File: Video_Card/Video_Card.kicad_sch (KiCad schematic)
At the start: 0 parts

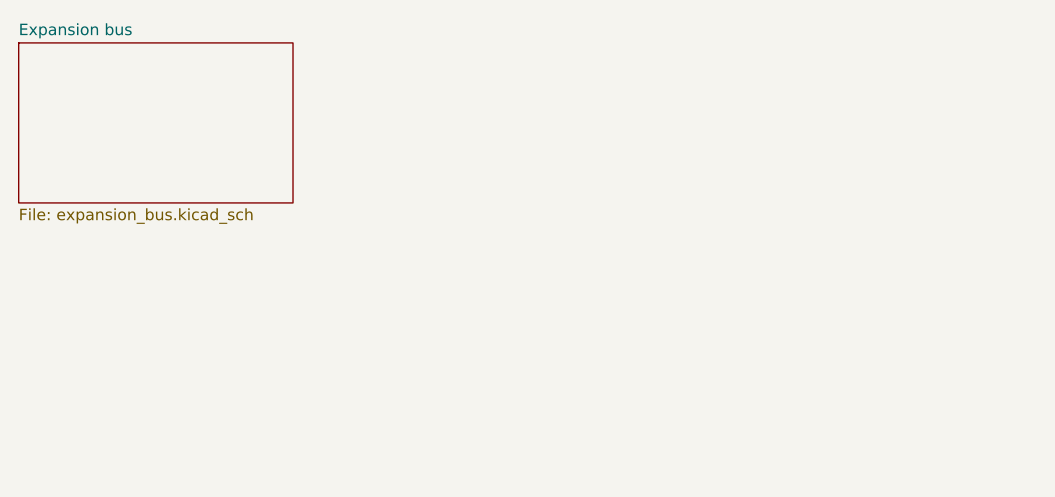
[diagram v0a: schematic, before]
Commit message: Work to date
Building out minimal required circuitry to interface FPGA to host system
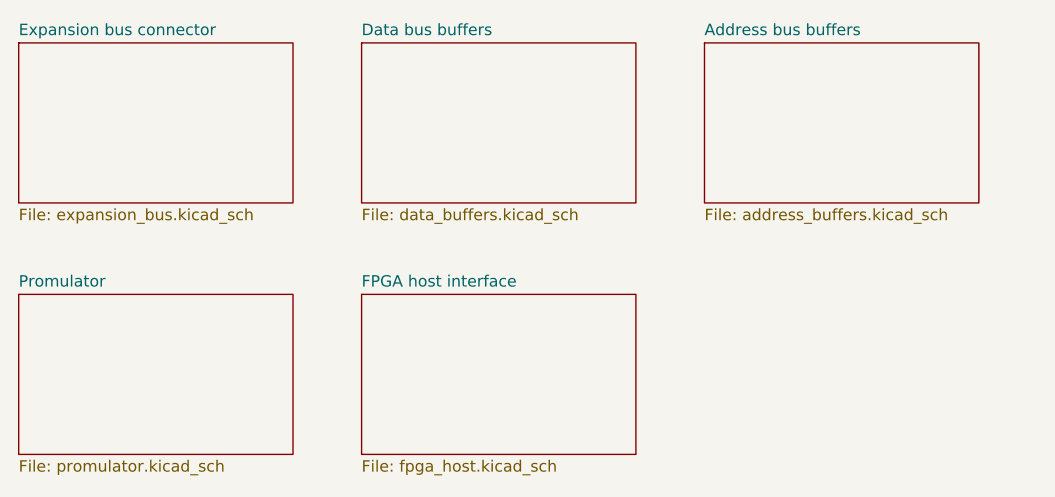
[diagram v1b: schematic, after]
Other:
- sheet Expansion bus renamed Expansion bus connector
- added sheet Address bus buffers (address_buffers.kicad_sch)
- added sheet Data bus buffers (data_buffers.kicad_sch)
- added sheet FPGA host interface (fpga_host.kicad_sch)
- added sheet Promulator (promulator.kicad_sch)
- title: COMET VIDEO CARD -> VGA COMPATIBLE VIDEO CARD
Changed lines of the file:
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@@
 	(paper "A4")
 	(title_block
-		(title "COMET VIDEO CARD")
+		(title "VGA COMPATIBLE VIDEO CARD")
 		(date "2025-03-30")
 		(rev "1")
 		(company "(C) TOM STOREY")
 		(comment 1 "FREE FOR NON-COMMERCIAL USE")
+	)
+	(sheet
+		(at 66.04 25.4)
+		(size 30.48 17.78)
+		(fields_autoplaced yes)
+		(stroke
+			(width 0.1524)
+			(type solid)
+		)
+		(fill
+			(color 0 0 0 0.0000)
+		)
+		(property "Sheetname" "Data bus buffers"
+			(at 66.04 24.6884 0)
+			(effects
+				(font
+					(size 1.27 1.27)
+				)
+				(justify left bottom)
+			)
+		)
+		(property "Sheetfile" "data_buffers.kicad_sch"
+			(at 66.04 43.7646 0)
+			(effects
+				(font
+					(size 1.27 1.27)
+				)
+				(justify left top)
+			)
+		)
+		(instances
+			(project "Video_Card"
+				(path "/ae665dca-cabf-48ec-b560-2bab32dde7c4"
+					(page "3")
+				)
+			)
+		)
+	)
+	(sheet
+		(at 66.04 53.34)
+		(size 30.48 17.78)
+		(fields_autoplaced yes)
+		(stroke
+			(width 0.1524)
+			(type solid)
+		)
+		(fill
+			(color 0 0 0 0.0000)
+		)
+		(property "Sheetname" "FPGA host interface"
+			(at 66.04 52.6284 0)
+			(effects
+				(font
+					(size 1.27 1.27)
+				)
+				(justify left bottom)
+			)
+		)
+		(property "Sheetfile" "fpga_host.kicad_sch"
+			(at 66.04 71.7046 0)
+			(effects
+				(font
+					(size 1.27 1.27)
+				)
+				(justify left top)
+			)
+		)
+		(instances
+			(project "Video_Card"
+				(path "/ae665dca-cabf-48ec-b560-2bab32dde7c4"
+					(page "6")
+				)
+			)
+		)
+	)
+	(sheet
+		(at 104.14 25.4)
+		(size 30.48 17.78)
+		(fields_autoplaced yes)
+		(stroke
+			(width 0.1524)
+			(type solid)
+		)
+		(fill
+			(color 0 0 0 0.0000)
+		)
+		(property "Sheetname" "Address bus buffers"
+			(at 104.14 24.6884 0)
+			(effects
+				(font
+					(size 1.27 1.27)
+				)
+				(justify left bottom)
+			)
+		)
+		(property "Sheetfile" "address_buffers.kicad_sch"
+			(at 104.14 43.7646 0)
+			(effects
+				(font
+					(size 1.27 1.27)
+				)
+				(justify left top)
+			)
+		)
+		(instances
+			(project "Video_Card"
+				(path "/ae665dca-cabf-48ec-b560-2bab32dde7c4"
+					(page "4")
+				)
+			)
+		)
+	)
+	(sheet
+		(at 27.94 53.34)
+		(size 30.48 17.78)
+		(fields_autoplaced yes)
+		(stroke
+			(width 0.1524)
+			(type solid)
+		)
+		(fill
+			(color 0 0 0 0.0000)
+		)
+		(property "Sheetname" "Promulator"
+			(at 27.94 52.6284 0)
+			(effects
+				(font
+					(size 1.27 1.27)
+				)
+				(justify left bottom)
+			)
+		)
+		(property "Sheetfile" "promulator.kicad_sch"
+			(at 27.94 71.7046 0)
+			(effects
+				(font
+					(size 1.27 1.27)
+				)
+				(justify left top)
+			)
+		)
+		(instances
+			(project "Video_Card"
+				(path "/ae665dca-cabf-48ec-b560-2bab32dde7c4"
+					(page "5")
+				)
+			)
+		)
 	)
 	(sheet
@@
 			(color 0 0 0 0.0000)
 		)
-		(property "Sheetname" "Expansion bus"
+		(property "Sheetname" "Expansion bus connector"
 			(at 27.94 24.6884 0)
 			(effects

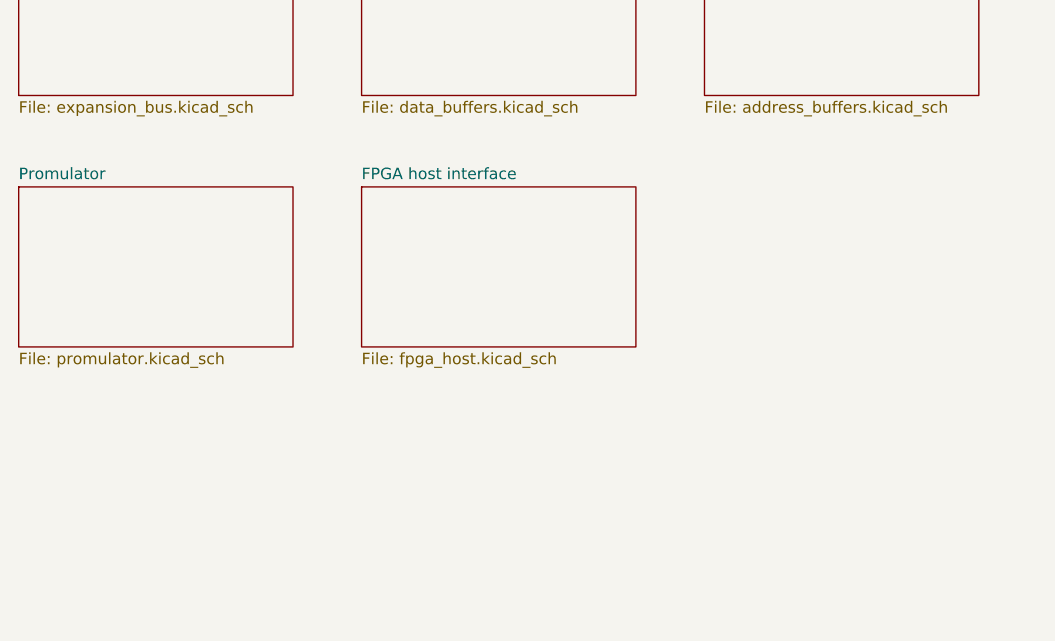
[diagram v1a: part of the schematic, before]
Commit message: Todays work:
* Added clock identifier to SPI flash clock input
* Add config pins to FPGA host interface - can be used for configuring address decoding
* Add FPGA clocks sheet
* Add expansion ROM sheet
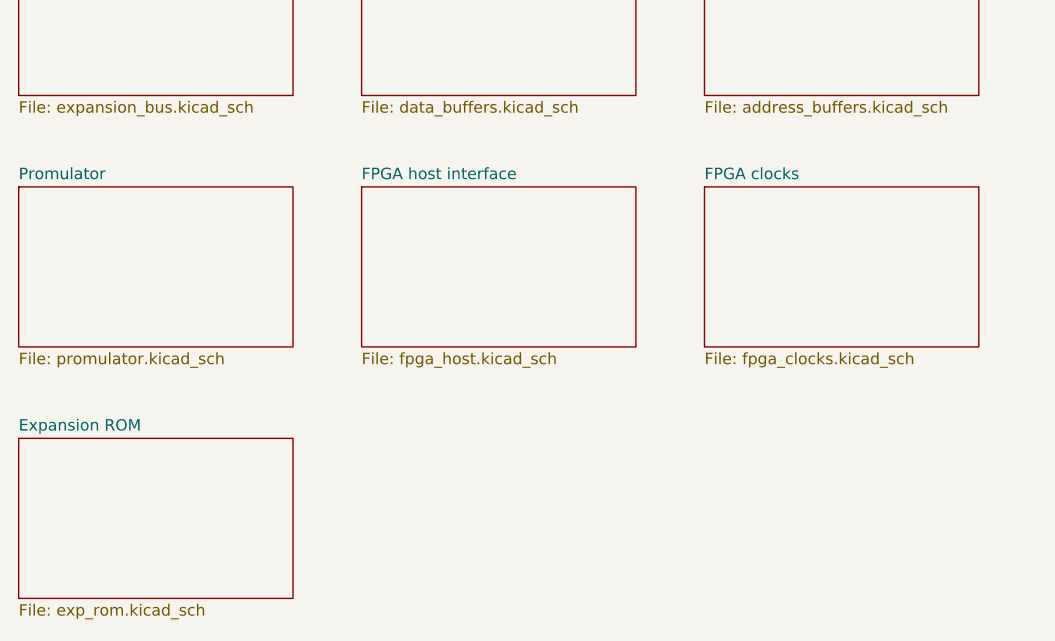
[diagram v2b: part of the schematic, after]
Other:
- added sheet Expansion ROM (exp_rom.kicad_sch)
- added sheet FPGA clocks (fpga_clocks.kicad_sch)
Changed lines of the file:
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@@
+	)
+	(sheet
+		(at 104.14 53.34)
+		(size 30.48 17.78)
+		(fields_autoplaced yes)
+		(stroke
+			(width 0.1524)
+			(type solid)
+		)
+		(fill
+			(color 0 0 0 0.0000)
+		)
+		(property "Sheetname" "FPGA clocks"
+			(at 104.14 52.6284 0)
+			(effects
+				(font
+					(size 1.27 1.27)
+				)
+				(justify left bottom)
+			)
+		)
+		(property "Sheetfile" "fpga_clocks.kicad_sch"
+			(at 104.14 71.7046 0)
+			(effects
+				(font
+					(size 1.27 1.27)
+				)
+				(justify left top)
+			)
+		)
+		(instances
+			(project "Video_Card"
+				(path "/ae665dca-cabf-48ec-b560-2bab32dde7c4"
+					(page "7")
+				)
+			)
+		)
 	)
 	(sheet
@@
 				)
 			)
+		)
+	)
+	(sheet
+		(at 27.94 81.28)
+		(size 30.48 17.78)
+		(fields_autoplaced yes)
+		(stroke
+			(width 0.1524)
+			(type solid)
+		)
+		(fill
+			(color 0 0 0 0.0000)
+		)
+		(property "Sheetname" "Expansion ROM"
+			(at 27.94 80.5684 0)
+			(effects
+				(font
+					(size 1.27 1.27)
+				)
+				(justify left bottom)
+			)
+		)
+		(property "Sheetfile" "exp_rom.kicad_sch"
+			(at 27.94 99.6446 0)
+			(effects
+				(font
+					(size 1.27 1.27)
+				)
+				(justify left top)
+			)
+		)
+		(instances
+			(project "Video_Card"
+				(path "/ae665dca-cabf-48ec-b560-2bab32dde7c4"
+					(page "8")
+				)
+			)

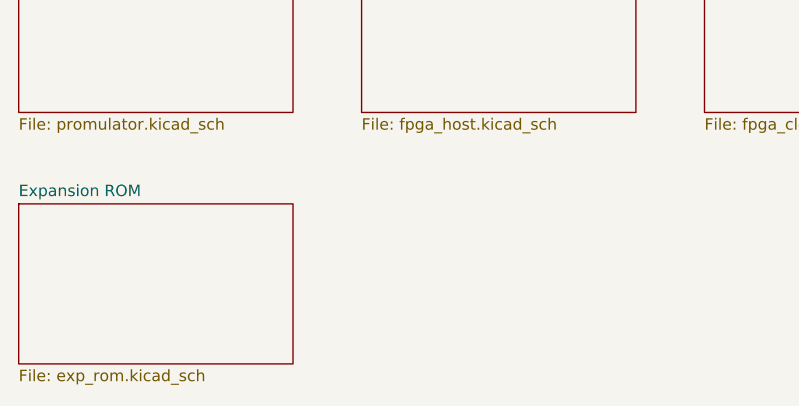
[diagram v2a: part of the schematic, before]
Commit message: Work to date:
* added RAMDAC sheet
* tweaks to promulator circuit to disconnect MCLR, and add future reset output
* tweaks to FPGA host interface, add pin numbers and rearrange reset input to allow reset either from the system or from the promulator following configuration
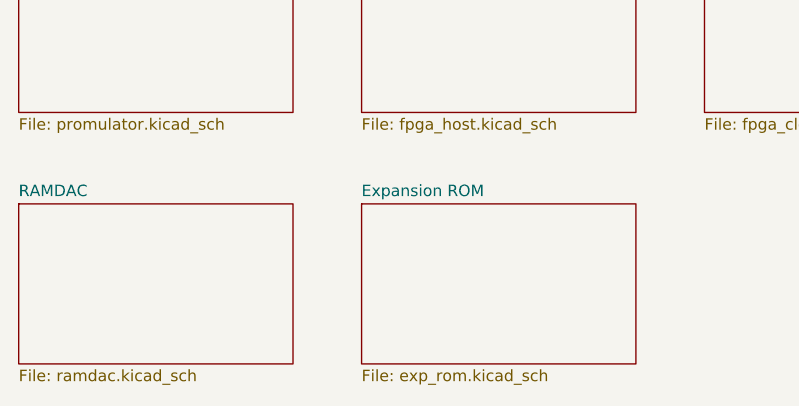
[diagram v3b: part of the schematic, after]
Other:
- added sheet RAMDAC (ramdac.kicad_sch)
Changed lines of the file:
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@@
+	)
+	(sheet
+		(at 27.94 81.28)
+		(size 30.48 17.78)
+		(fields_autoplaced yes)
+		(stroke
+			(width 0.1524)
+			(type solid)
+		)
+		(fill
+			(color 0 0 0 0.0000)
+		)
+		(property "Sheetname" "RAMDAC"
+			(at 27.94 80.5684 0)
+			(effects
+				(font
+					(size 1.27 1.27)
+				)
+				(justify left bottom)
+			)
+		)
+		(property "Sheetfile" "ramdac.kicad_sch"
+			(at 27.94 99.6446 0)
+			(effects
+				(font
+					(size 1.27 1.27)
+				)
+				(justify left top)
+			)
+		)
+		(instances
+			(project "Video_Card"
+				(path "/ae665dca-cabf-48ec-b560-2bab32dde7c4"
+					(page "8")
+				)
+			)
+		)
 	)
 	(sheet
@@
 	)
 	(sheet
-		(at 27.94 81.28)
+		(at 66.04 81.28)
 		(size 30.48 17.78)
 		(fields_autoplaced yes)
@@
 		)
 		(property "Sheetname" "Expansion ROM"
-			(at 27.94 80.5684 0)
+			(at 66.04 80.5684 0)
 			(effects
 				(font
@@
 		)
 		(property "Sheetfile" "exp_rom.kicad_sch"
-			(at 27.94 99.6446 0)
+			(at 66.04 99.6446 0)
 			(effects
 				(font
@@
 			(project "Video_Card"
 				(path "/ae665dca-cabf-48ec-b560-2bab32dde7c4"
-					(page "8")
+					(page "9")
 				)
 			)

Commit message: Progress as of returning from travel
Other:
- added sheet Regen bus mux (regen_bus_mux.kicad_sch)
- added sheet Regen memory banks (regen_mem.kicad_sch)
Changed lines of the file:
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@@
+	)
+	(sheet
+		(at 66.04 109.22)
+		(size 30.48 17.78)
+		(fields_autoplaced yes)
+		(stroke
+			(width 0.1524)
+			(type solid)
+		)
+		(fill
+			(color 0 0 0 0.0000)
+		)
+		(property "Sheetname" "Regen memory banks"
+			(at 66.04 108.5084 0)
+			(effects
+				(font
+					(size 1.27 1.27)
+				)
+				(justify left bottom)
+			)
+		)
+		(property "Sheetfile" "regen_mem.kicad_sch"
+			(at 66.04 127.5846 0)
+			(effects
+				(font
+					(size 1.27 1.27)
+				)
+				(justify left top)
+			)
+		)
+		(instances
+			(project "Video_Card"
+				(path "/ae665dca-cabf-48ec-b560-2bab32dde7c4"
+					(page "11")
+				)
+			)
+		)
 	)
 	(sheet
@@
 				)
 			)
+		)
+	)
+	(sheet
+		(at 27.94 109.22)
+		(size 30.48 17.78)
+		(fields_autoplaced yes)
+		(stroke
+			(width 0.1524)
+			(type solid)
+		)
+		(fill
+			(color 0 0 0 0.0000)
+		)
+		(property "Sheetname" "Regen bus mux"
+			(at 27.94 108.5084 0)
+			(effects
+				(font
+					(size 1.27 1.27)
+				)
+				(justify left bottom)
+			)
+		)
+		(property "Sheetfile" "regen_bus_mux.kicad_sch"
+			(at 27.94 127.5846 0)
+			(effects
+				(font
+					(size 1.27 1.27)
+				)
+				(justify left top)
+			)
+		)
+		(instances
+			(project "Video_Card"
+				(path "/ae665dca-cabf-48ec-b560-2bab32dde7c4"
+					(page "10")
+				)
+			)
